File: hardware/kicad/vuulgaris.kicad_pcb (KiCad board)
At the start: 4 copper layers, 284.3 x 116.8 mm, 279 parts, among them J1 TFPUSH, J10 PJ-603_C41409498, J11 TYPE-C-31-M-12, J12 FACEPLATE 2x5 IDC, J2 PJ-376, J3 PJ-376, J4 PJ-376, J5 PJ-376, J7 PJ-603_C41409498, J8 PJ-603_C41409498, J9 PJ-603_C41409498, Q1 J113 / MMBFJ113, Q2 J113 / MMBFJ113, SW1 SW_DPDT_FLAT, SW2 SW_DPDT_FLAT, SW4 12x12 tactile, SW5 12x12 tactile, SW6 12x12 tactile, SW7 12x12 tactile, SW8 12x12 tactile, SW9 12x12 tactile, U1 ES_DAISY_PATCH_SM_REV1, U101 V3205SD, U102 TL072_FLAT, U103 TL072_FLAT, U104 CD4046B, U106 TL072_FLAT, U201 V3205SD, U202 TL072_FLAT, U203 TL072_FLAT, U204 CD4046B, U206 TL072_FLAT, U3 MCP23017-E_SO, U301 TL084, U302 TL074, U4 MCP23017-E_SO, U401 TL084, U402 TL074, U5 AMS1117-3.3, U6 AMS1117-3.3, U7 DKM10E-12, U8 78L05

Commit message: hardware: LPG trimmers to SMD 3224W, mounted on the back
RT301/RT401 go from Bourns 3266W (through-hole, no LCSC number at all) to
3224W-1-203E, LCSC C55071 -- the SMD sibling: same 4mm square multiturn cermet,
12 turns, top-adjust, 9784 in stock. Footprint pulled with easyeda2kicad. Pin
numbering matches TRIMPOT_3T, so the rheostat wiring is unchanged.

Multiturn was the constraint. These set vactrol LED drive depth by ear against a
scope; the 3x3mm single-turn parts are cheaper and better stocked but put 20k
into 270 degrees.

Mounted on B.Cu rather than with the rest of the LPG on F.Cu: the front is under
the faceplate, so a top-adjust trimmer there is only reachable with the panel
off, and vactrols age. Flip verified against the library by place.py's pad
orientation check (700 pads, 0 wrong) and in the plotted gerbers (3 B.Cu flashes
at RT301).

Takes the hand-solder list from 12 parts to 10; what remains has no LCSC source.

864/864 verified, no pad overlaps, nothing within 1.5mm of a chip pad.
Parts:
- RT301, RT401: footprint vuulgaris:Potentiometer_Bourns_3266W_Vertical -> vuulgaris:RES-ADJ-SMD_3224W; moved to B.Cu
- moved RT401 50.8 mm to (220.4, 150.9)
- moved RT301 48.9 mm to (220.4, 115.5)

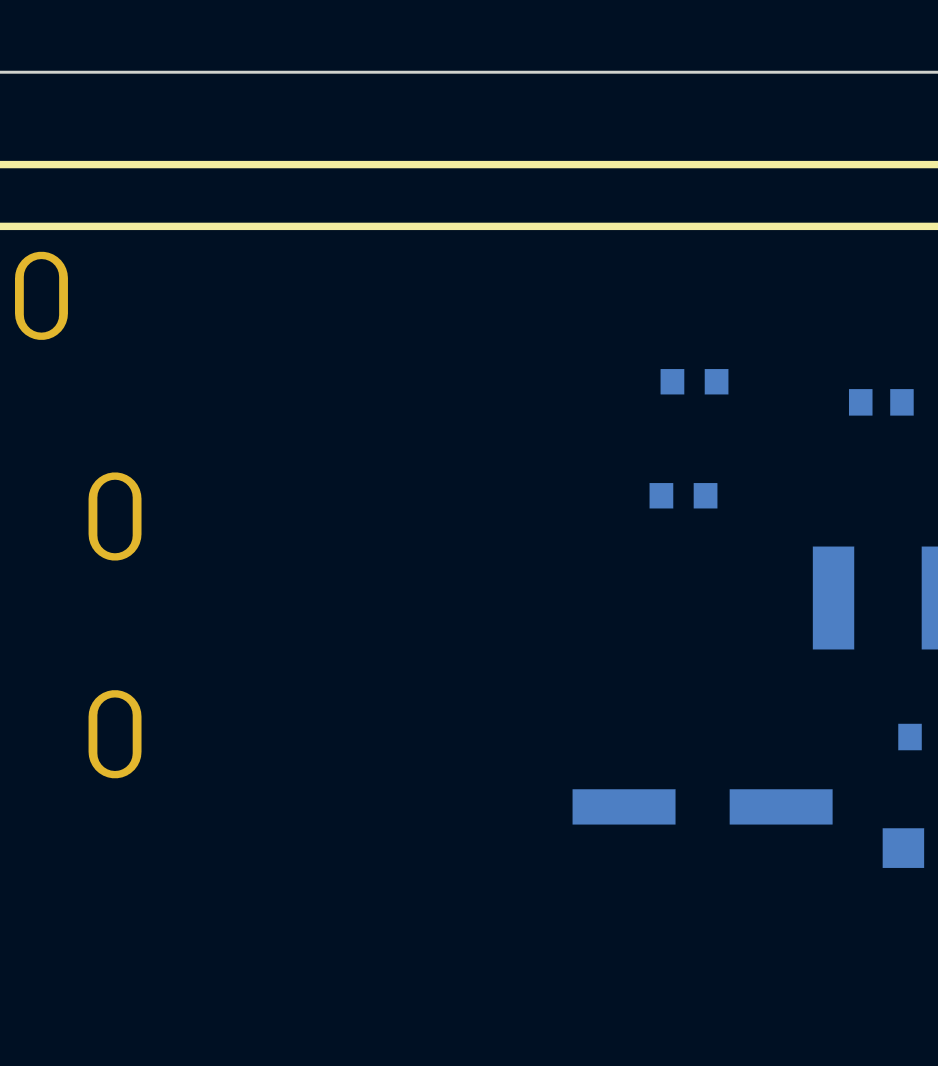
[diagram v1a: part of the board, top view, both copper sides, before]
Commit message: hardware: headphone monitor output -- OPA1688 driver and J6
J6 (PJ-376, already a stereo TRS: 1 sleeve, 2 ring, 3 tip) on the top wall
immediately right of J10, tucked under the OLED on B.Cu as J9/J10 already are.

U9 is an OPA1688 (C206212) rather than the NJM4556A first proposed -- same
supply range and 75mA drive, but TI characterise 0.00005 percent THD+N INTO 32
ohms and TIPD189 is their headphone-amp reference design on it. Two orders of
magnitude better distortion.

Its LCSC symbol is multi-unit (pins 1/7, 2/6, 3/5 share coordinates) and would
have stubbed OUTA onto OUTB in mksch, so OPA1688_FLAT is cloned from TL072_FLAT,
whose pinout is identical. Same trap the other FLAT symbols exist for.

Taps BBD_OUT -- what the quarter-inch jacks and the resample leg see -- through
1uF, 100k, a 20k trimmer to ground, a unity buffer and 22R. Max ratio 0.167,
roughly 10mW into 32 ohms; the trimmers bring it down and are set once. No
dual-gang SMD trimmer is in stock anywhere, so there are two, against bbd-mki's
advice about L/R matching: set them with a meter, not by ear.

Two things the placement seeds cannot express, fixed in the board:

- the block belongs on B.Cu; seeded parts arrive on F.Cu and sat on the OLED
- J6 needs rotation -90 like every other jack. At rotation 0 the PJ-376 body
  runs 24mm in -x and lands on J10 -- caught by the body-overlap check. The
  pad-orientation check then caught that rotating a footprint also has to update
  its stored ABSOLUTE pad angles: J5 stores 270, J6 had 0, and the pads are
  1.6x3.1 rectangles so the difference is real copper.

897/897 verified, 0 unintended. Body overlaps back to the three pre-existing.
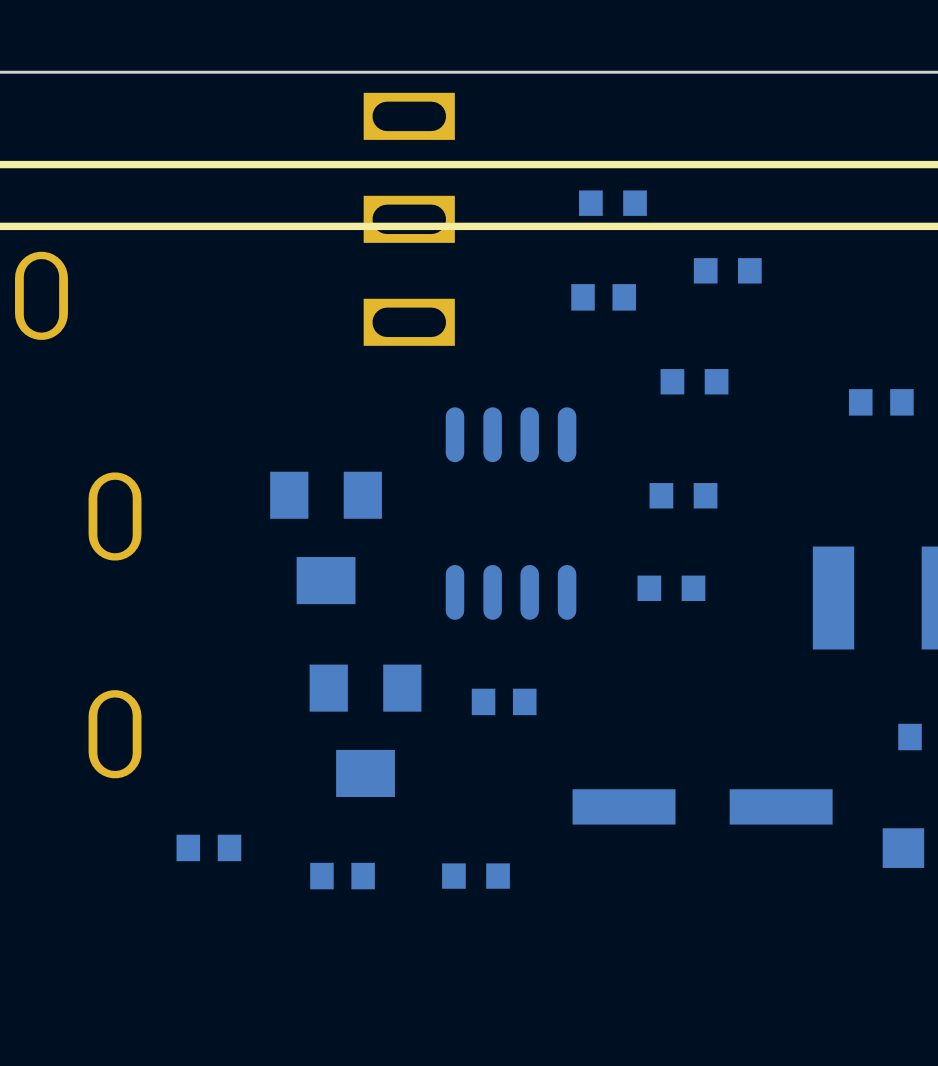
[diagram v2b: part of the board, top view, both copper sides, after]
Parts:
- added C505: 1uF film, vuulgaris:C0603, B.Cu at (347.1, 57.7)
- added C506: 1uF film, vuulgaris:C0603, B.Cu at (343.7, 71.4)
- added C507: 100nF, vuulgaris:C0603, B.Cu at (338.2, 77.3)
- added C508: 100nF, vuulgaris:C0603, B.Cu at (333.7, 76.4)
- added J6: PJ-376, vuulgaris:AUDIO-TH_PJ-376, B.Cu at (340.5, 55.0)
- added R509: 100k, vuulgaris:R0603, B.Cu at (349.4, 67.5)
- added R510: 100k, vuulgaris:R0603, B.Cu at (347.4, 54.5)
- added R511: 22R, vuulgaris:R0603, B.Cu at (351.3, 56.8)
- added R512: 22R, vuulgaris:R0603, B.Cu at (342.8, 77.3)
- added RT501: 20k trim, vuulgaris:RES-ADJ-SMD_3224W, B.Cu at (337.7, 65.8)
- added RT502: 20k trim, vuulgaris:RES-ADJ-SMD_3224W, B.Cu at (339.0, 72.4)
- added U9: OPA1688_FLAT, vuulgaris:SOP-8_L4.9-W3.9-P1.27-LS6.0-BL, B.Cu at (344.0, 65.0)

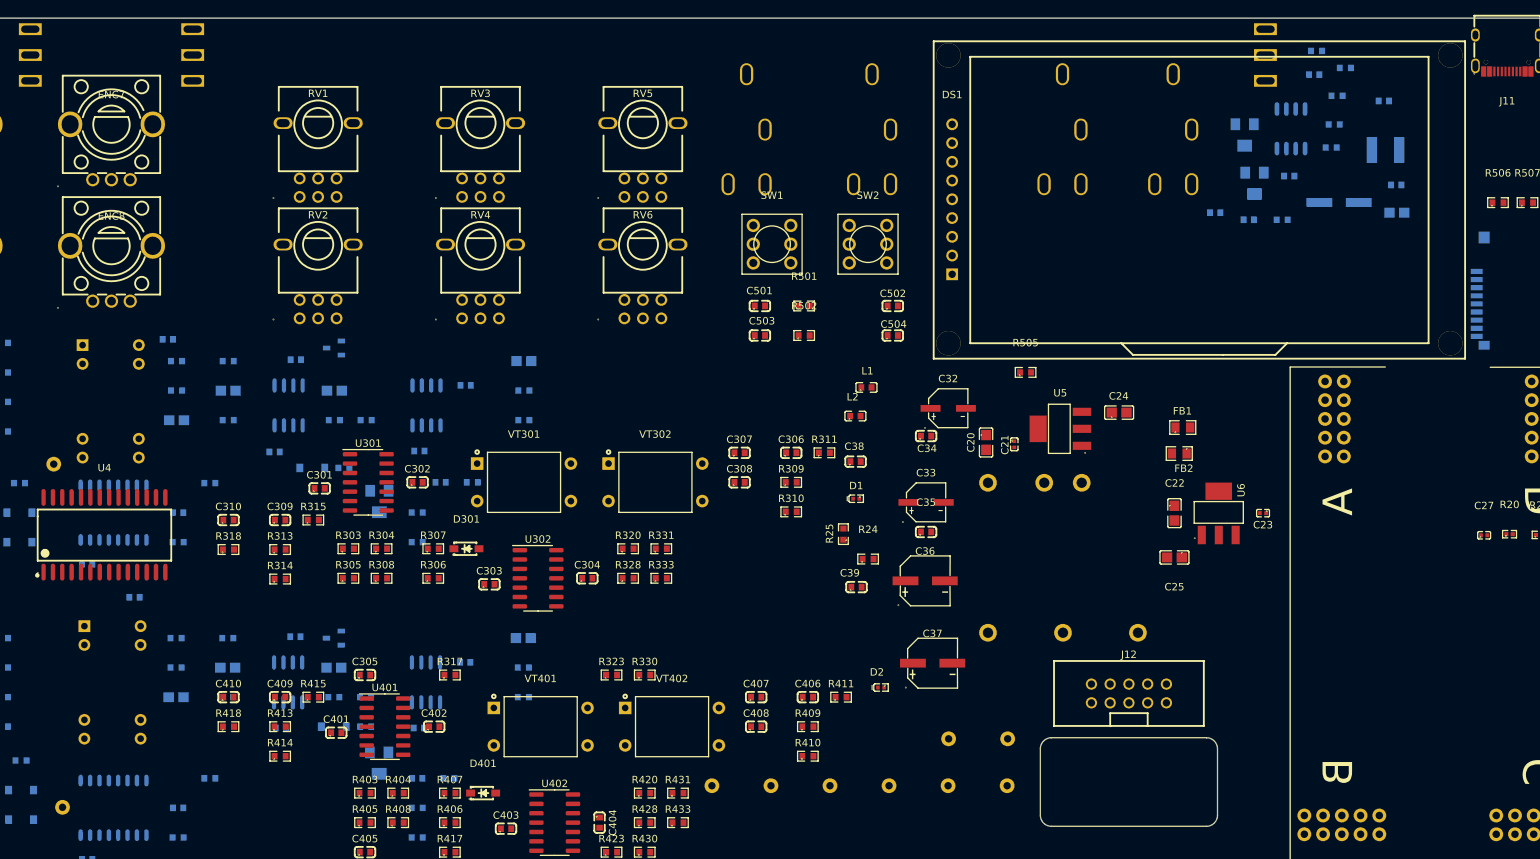
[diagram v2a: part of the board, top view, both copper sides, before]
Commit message: hardware: drop the 1/4" outs to line level, fix the headphone series R
The 1/4" outs sat straight on BBD_OUT at Eurorack level, 9.5Vpp / +12.7dBu.
That survives a pro interface but clips consumer gear and anything with an
instrument input. R513-R516 divide it to +3.9dBu full scale.

The divider sits downstream of the C503 (resample) and C505 (headphone) taps,
so BBD_OUT keeps the Eurorack level the internal chain is matched to and only
the jack moves. With R131's existing 470R the ratio is 1000/2770 = -8.85dB,
639R out, 2770R load on U103 -- inside the TL072's 2k rating.

R511/R512 22R -> 4R7. They are outside U9's feedback loop, so they set output
impedance directly: 22R into 32R cans is damping factor 1.5, which colours the
bass differently for every pair, and throws away 4.6dB. The OPA1688 is a
headphone driver with internal short-circuit protection and does not need the
isolation.

pose.py is new. place.py owns X/Y but not layer or rotation, so every F8 drops
re-imported footprints back on F.Cu at 0 degrees -- that has eaten the bypass
caps once and the headphone block twice. pose.py snapshots and restores all
295 poses; verified by clobbering the 160 non-default ones and restoring
byte-identical. It derives pad angles from the board rather than the library,
because a library lookup miss invents a rotation out of nothing.

Documented that back-side silkscreen text is unmirrored on ~160 parts: 324
fp_text entries disagree with their own layer, so back reference designators
will plot reversed. Cosmetic, not fixed here.
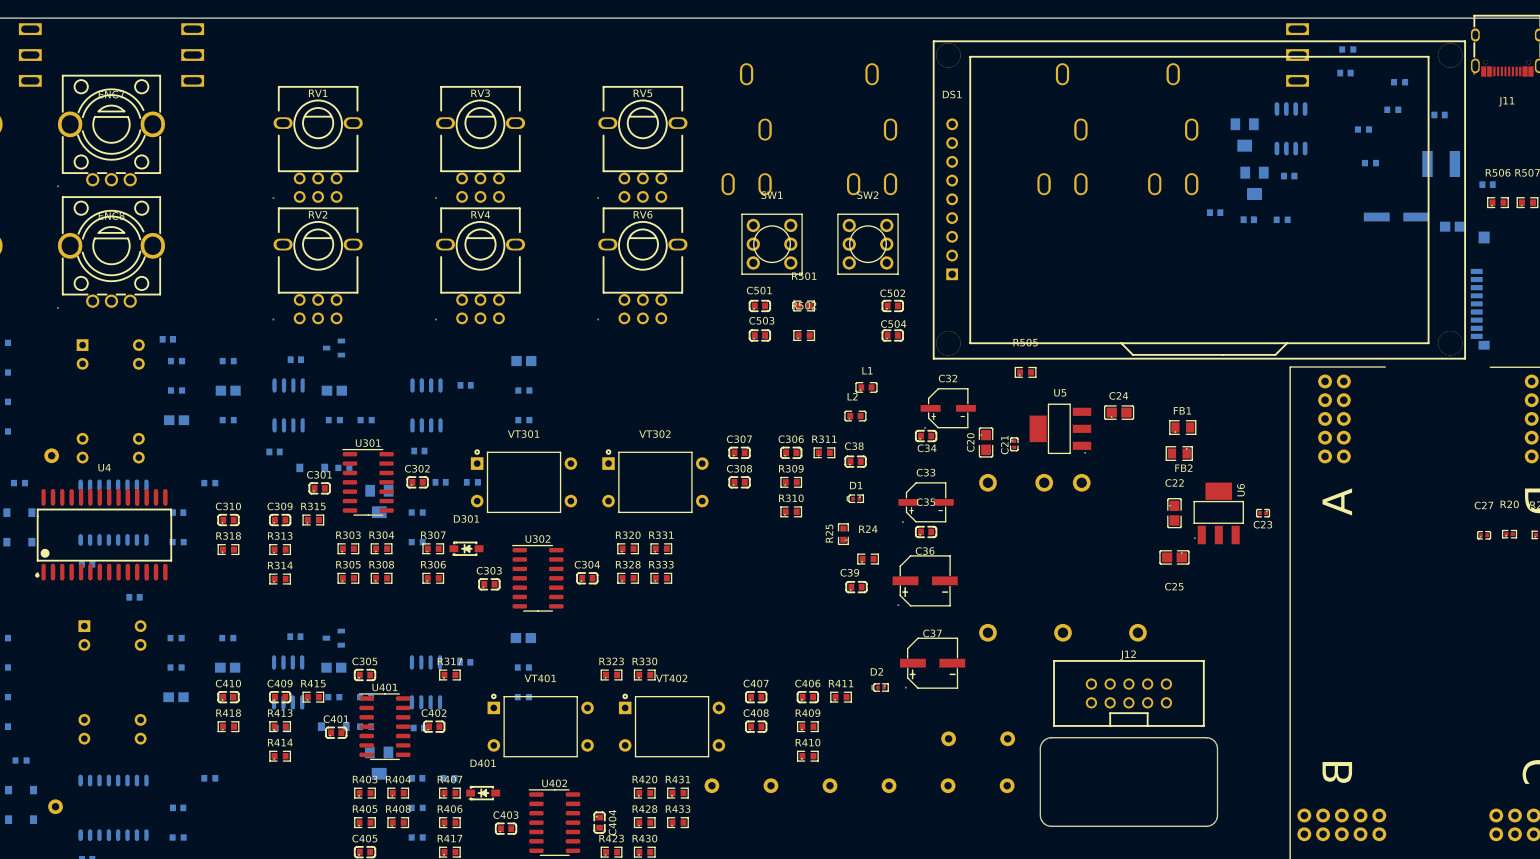
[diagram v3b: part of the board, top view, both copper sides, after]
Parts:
- moved C31 12.4 mm to (370.6, 72.5)
- moved C29 8.02 mm to (358.2, 76.9)
- moved C28 7.79 mm to (364.1, 63.1)
- moved R22 7.79 mm to (357.7, 62.4)
- moved C30 7.79 mm to (365.8, 78.3)
- moved F1 7.79 mm to (364.3, 69.8)
- moved R511 7.60 mm to (358.7, 58.7)
- moved R509 5.71 mm to (354.7, 69.6)
- moved J6 4.35 mm to (344.8, 55.0)
- moved C505 4.22 mm to (351.3, 57.4)
- moved R510 4.22 mm to (351.6, 54.2)
- moved R23 4.01 mm to (353.8, 65.1)
- moved TP12 1.17 mm to (176.0, 109.3)
- moved TP13 0.95 mm to (176.6, 156.8)

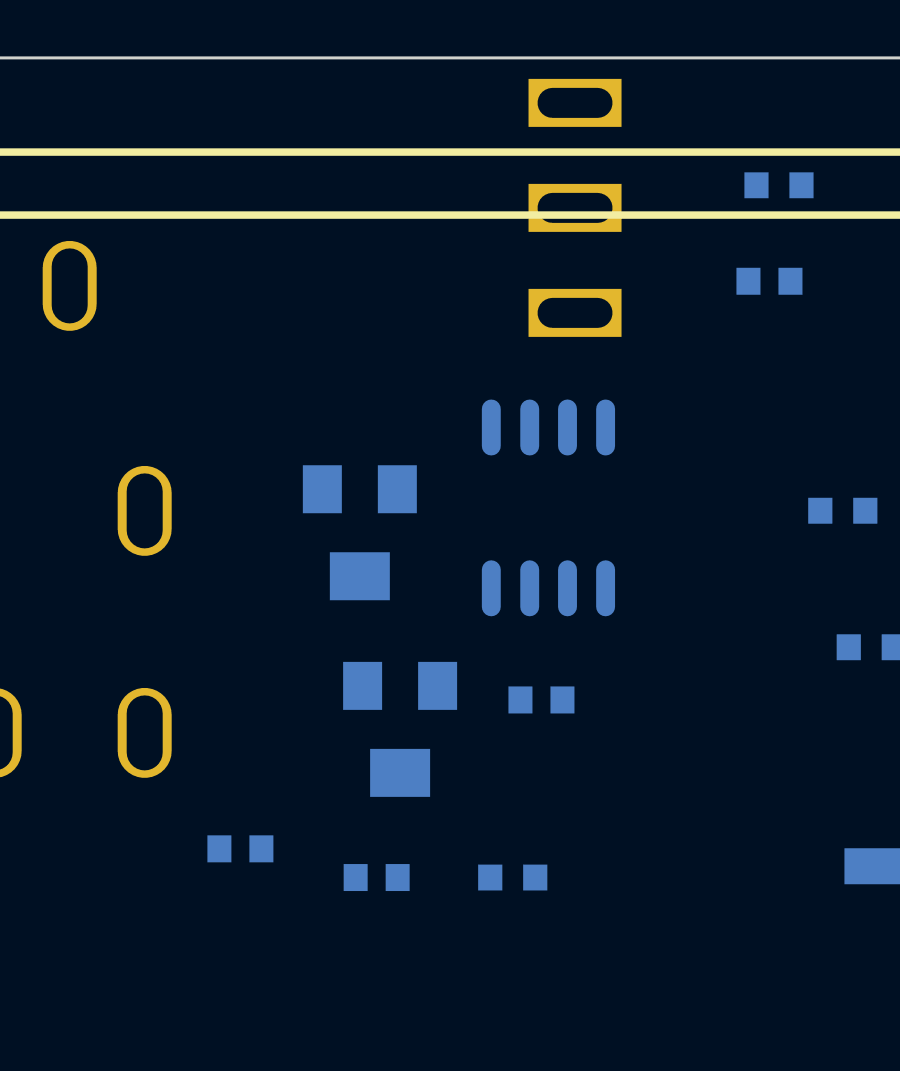
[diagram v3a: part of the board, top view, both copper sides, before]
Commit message: hardware: EXT input preamp, and U9's bypass caps were 15mm away
The 1/4" inputs fed U1.B3/B4 through a coupling cap and nothing else, at unity.
The Patch SM's full scale is Eurorack 9.5Vpp, so a receiver lands at -20dBFS and
a phone at -10dBFS. Software gain does not recover that -- it lifts the
converter's noise floor with the signal.

U10 is a second OPA1688, non-inverting, with RT503/RT504 in the feedback leg
giving 1x to 10.1x. It sits before SW2 so only the EXT branch is gained; the
resample path keeps its Eurorack level. C501 already blocks DC into the switch,
so the feedback leg needs no cap and U10's offset never reaches the module. At
minimum trim the stage is a unity follower, so a hot source is still safe.

R517/R518 1k are series protection off the jacks. There was none at all -- C501
went straight onto a module pin, and a source peaking at +18dBu is 17.4Vpp
against a +/-4.75V input. Against R519's 100k the 1k costs under 0.1dB.

Adding U9 and U10 to place.py's BYPASS table caught C507/C508 sitting 15.5mm and
15.0mm from the pins they decouple -- they were never in the table, so the check
had been auditing only the parts that were already right. RT502 moves 7.5mm off
U9 pin 8 to free the pocket; both caps are now inside 2.5mm.

The slot finder used for all of this had the back-side mirror wrong: place.py
negates local Y for B.Cu footprints and the finder did not, so every proposed
position was judged against mirrored neighbours. It also required quoted pad
names, which the library files do not use, so candidates came back with no
geometry at all and passed. Both fixed, and the placements redone -- R513-R516
moved as a result.
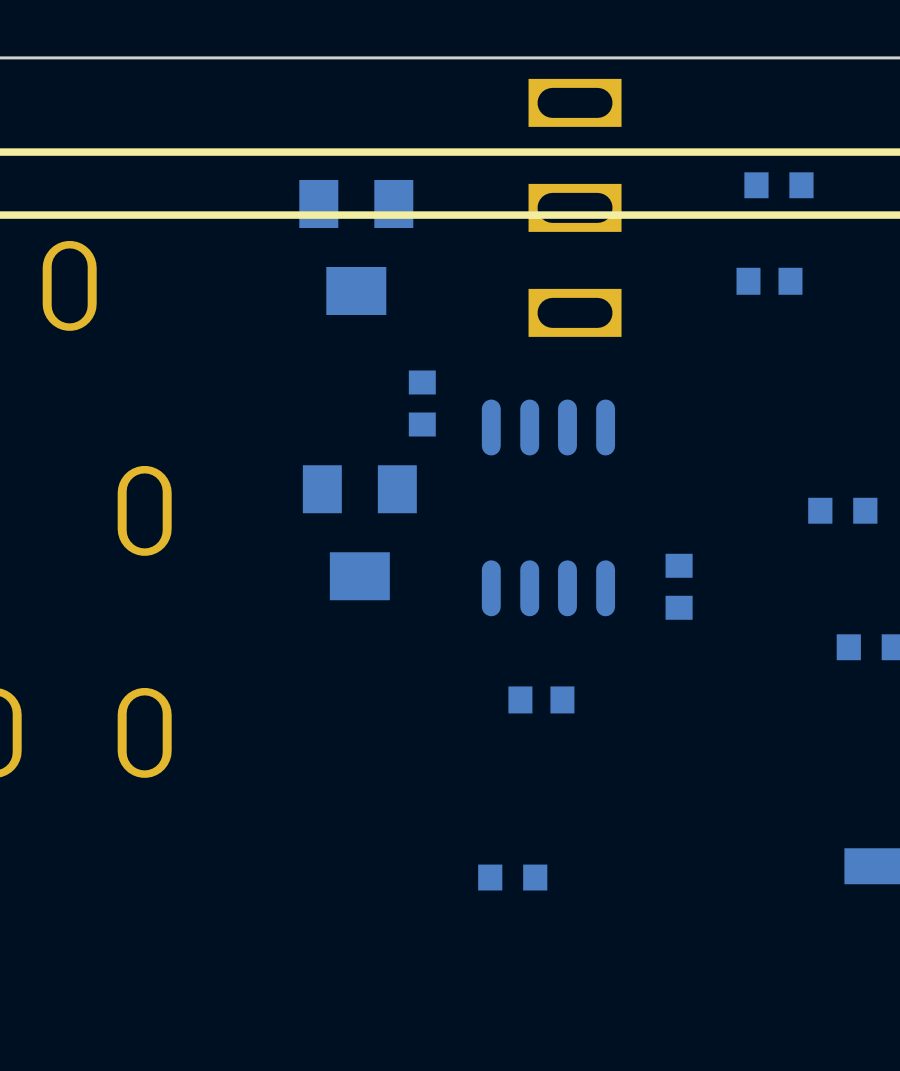
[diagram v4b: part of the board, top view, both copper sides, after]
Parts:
- moved C508 17.0 mm to (348.3, 67.6), turned to 90 degrees
- moved RT502 16.1 mm to (337.6, 56.3)
- moved C507 15.9 mm to (339.8, 61.5), turned to 90 degrees
